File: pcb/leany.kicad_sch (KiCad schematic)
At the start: 42 parts, among them J1 ST7735S, J2 SWD, Q1 AO3401A, SW1 ZERO, SW2 HOLD, SW3 RESET, SW4 BOOT, U1 STM32F103C8Tx, U2 CH340N, U3 ICM-42688-P, Y1 8MHz

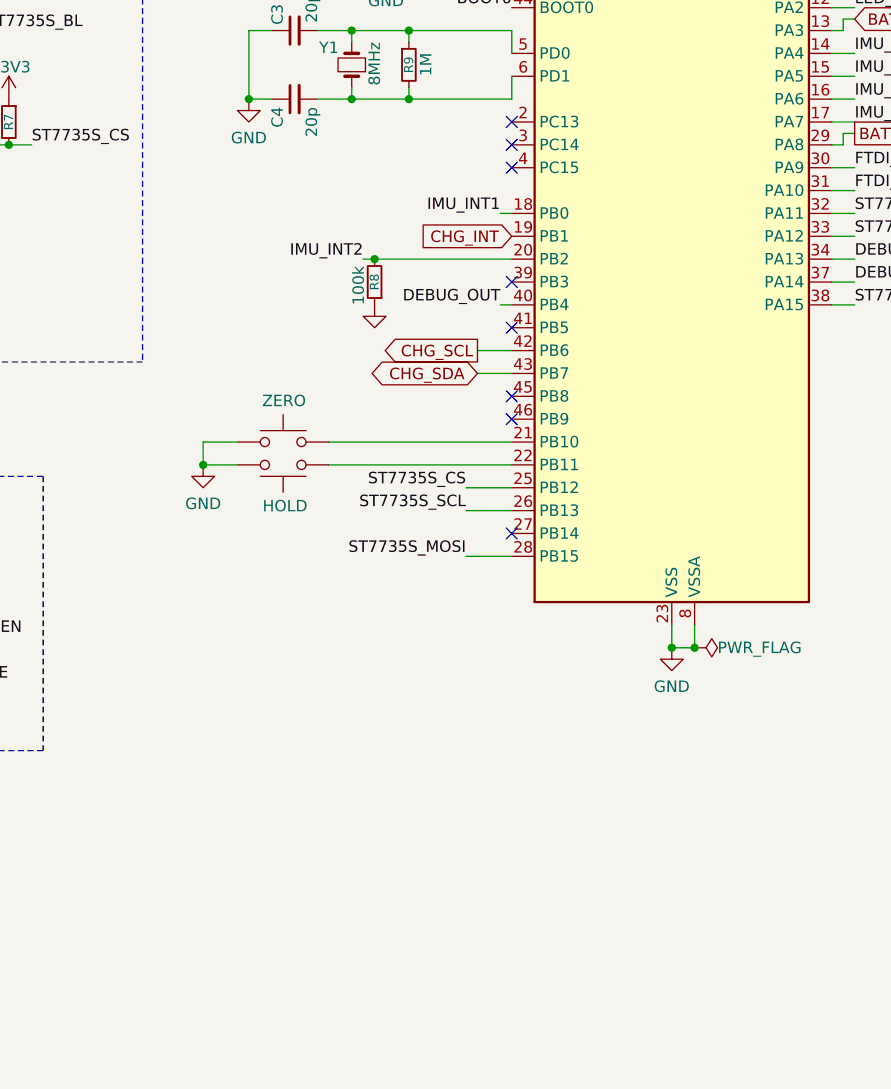
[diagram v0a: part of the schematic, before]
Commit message: feat: place and route external eeprom (#90)
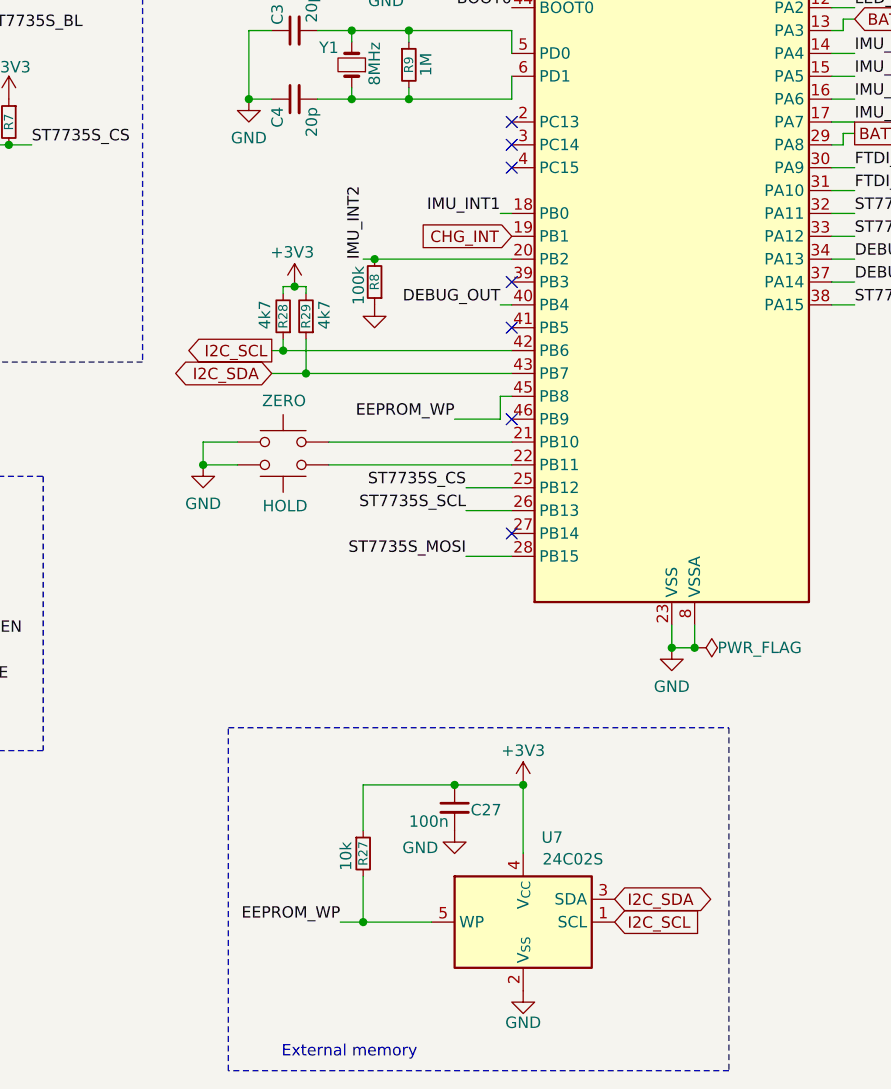
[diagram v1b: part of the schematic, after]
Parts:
- added C27: 100n, leany_footprints:C_0402_1005Metric, symbol leany-symbols:C_Small
- added R27: 10k, leany_footprints:R_0402_1005Metric, symbol Device:R_Small
- added R28, R29: 4k7, leany_footprints:R_0402_1005Metric, symbol Device:R_Small
- added U7: 24C02S, Package_TO_SOT_SMD:SOT-23-5, symbol leany-symbols:24C02S
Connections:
- net +3V3: now also C27.1, R27.1, R28.2, R29.2, U7.4 (V_{CC})
- net GND: now also C27.2, U7.2 (V_{SS})
- net EEPROM_WP: now reaches U1.45 (PB8)
- net EEPROM_WP: now also R27.2, U7.5 (WP)
- net CHG_SCL renamed I2C_SCL
- net I2C_SCL: now also R28.1, U7.1 (SCL)
- net CHG_SDA renamed I2C_SDA
- net I2C_SDA: now also R29.1, U7.3 (SDA)
- no-connect marks 9 -> 8
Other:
- note added: "External memory"

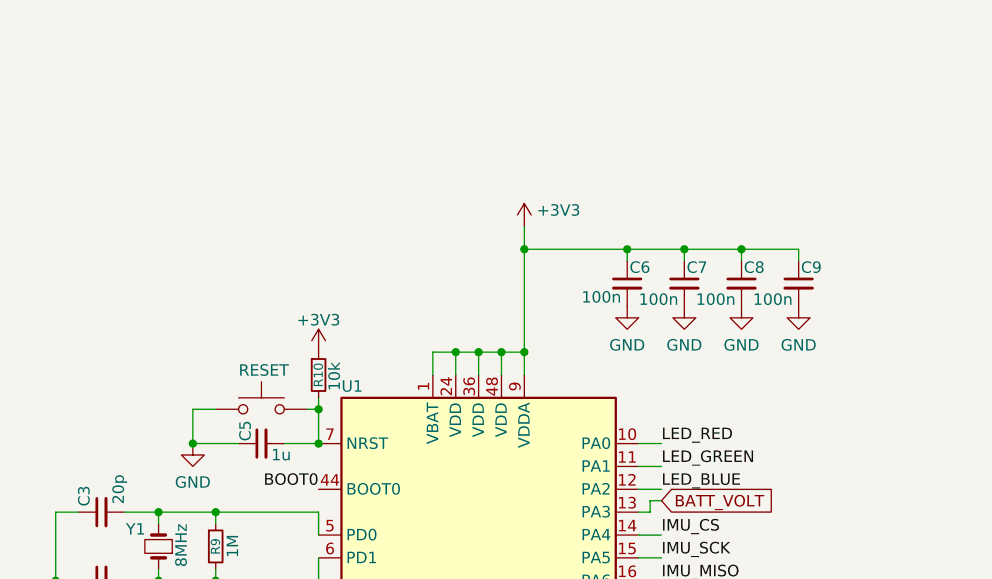
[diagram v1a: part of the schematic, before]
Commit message: refactor: improve STM32 decoupling (#90)
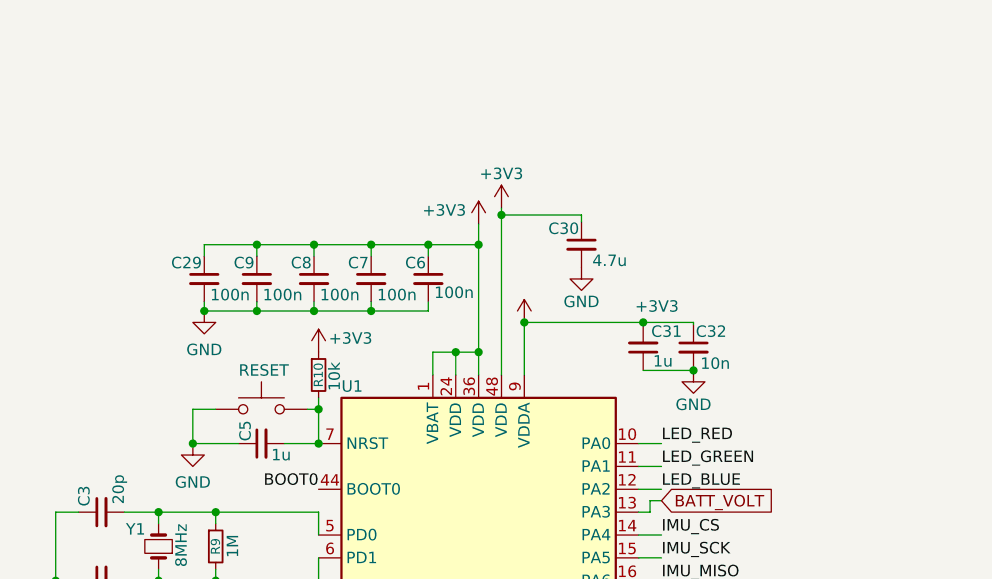
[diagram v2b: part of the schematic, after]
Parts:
- added C29: 100n, leany_footprints:C_0402_1005Metric, symbol leany-symbols:C_Small
- added C30: 4.7u, leany_footprints:C_0402_1005Metric, symbol leany-symbols:C_Small
- added C31: 1u, leany_footprints:C_0402_1005Metric, symbol leany-symbols:C_Small
- added C32: 10n, leany_footprints:C_0402_1005Metric, symbol leany-symbols:C_Small
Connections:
- net +3V3: now also C29.1, C30.1, C31.2, C32.1
- net GND: now also C29.2, C30.2, C31.1, C32.2
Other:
- moved on the sheet: C6, C7, C8, C9

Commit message: refactor: beef up the crystal load capacitors (#90)
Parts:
- C3, C4: value 20p -> 33p; LCSC C1554 -> C1562
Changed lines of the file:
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@@
 			)
 		)
-		(property "Value" "20p"
+		(property "Value" "33p"
 			(at 93.345 86.36 0)
 			(show_name no)
@@
 			)
 		)
-		(property "LCSC" "C1554"
+		(property "LCSC" "C1562"
 			(at 91.44 83.82 0)
 			(hide yes)
@@
 			)
 		)
-		(property "Value" "20p"
+		(property "Value" "33p"
 			(at 93.345 73.66 0)
 			(show_name no)
@@
 			)
 		)
-		(property "LCSC" "C1554"
+		(property "LCSC" "C1562"
 			(at 91.44 76.2 0)
 			(hide yes)
